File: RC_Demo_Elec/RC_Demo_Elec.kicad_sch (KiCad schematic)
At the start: 4 parts, among them M1 Motor_DC_LEFT, M2 Motor_DC_RIGHT, U1 Nucleo-L152RE

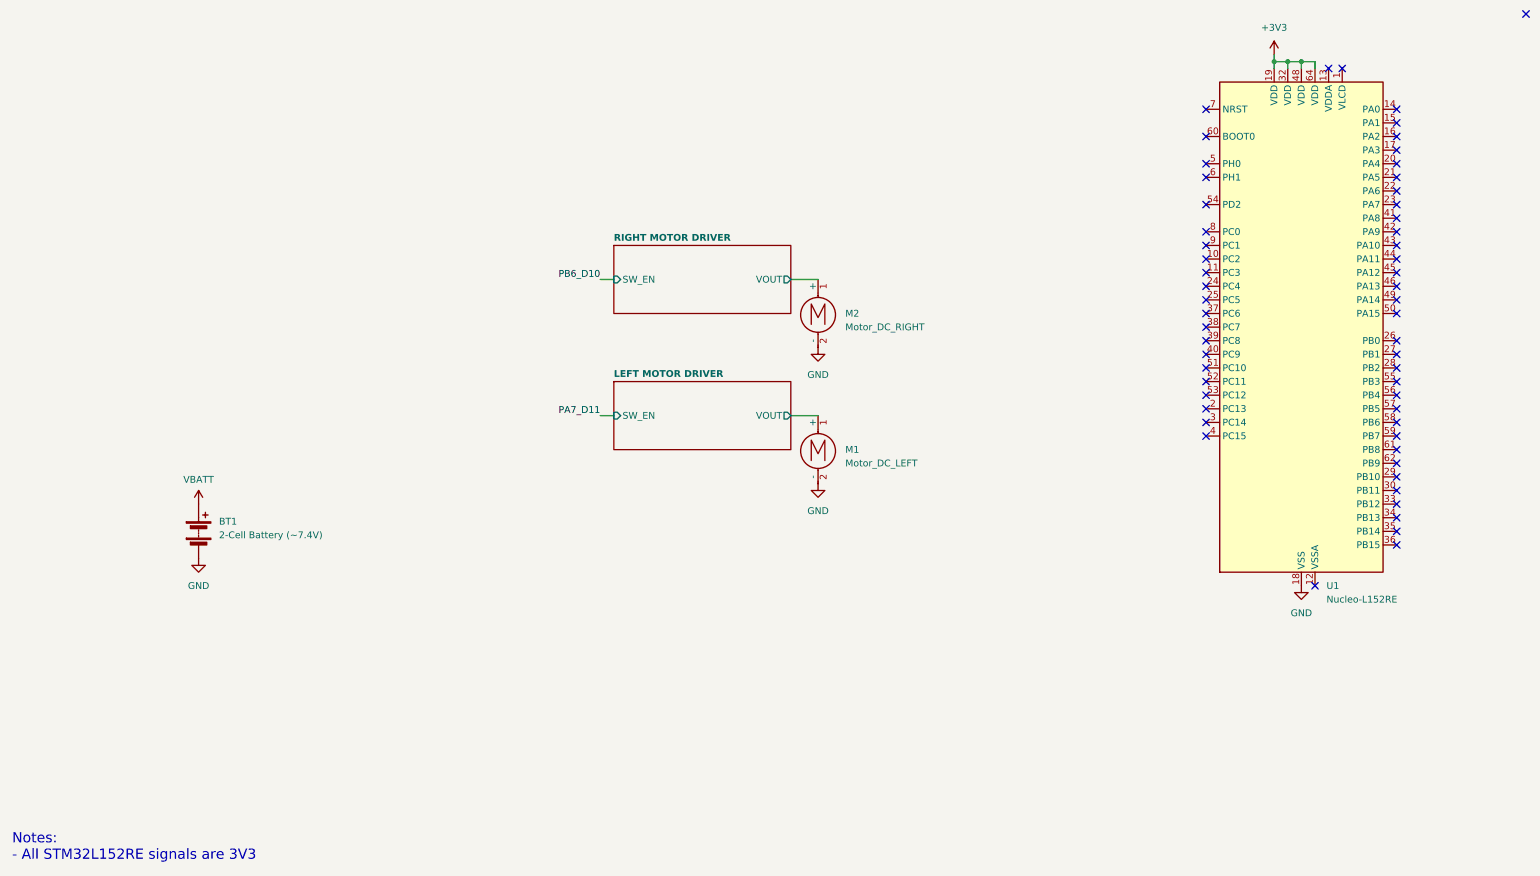
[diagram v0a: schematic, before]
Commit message: [chore] - pin ThetOS to v1.1.0 + commit Cargo.lock + schematic added note
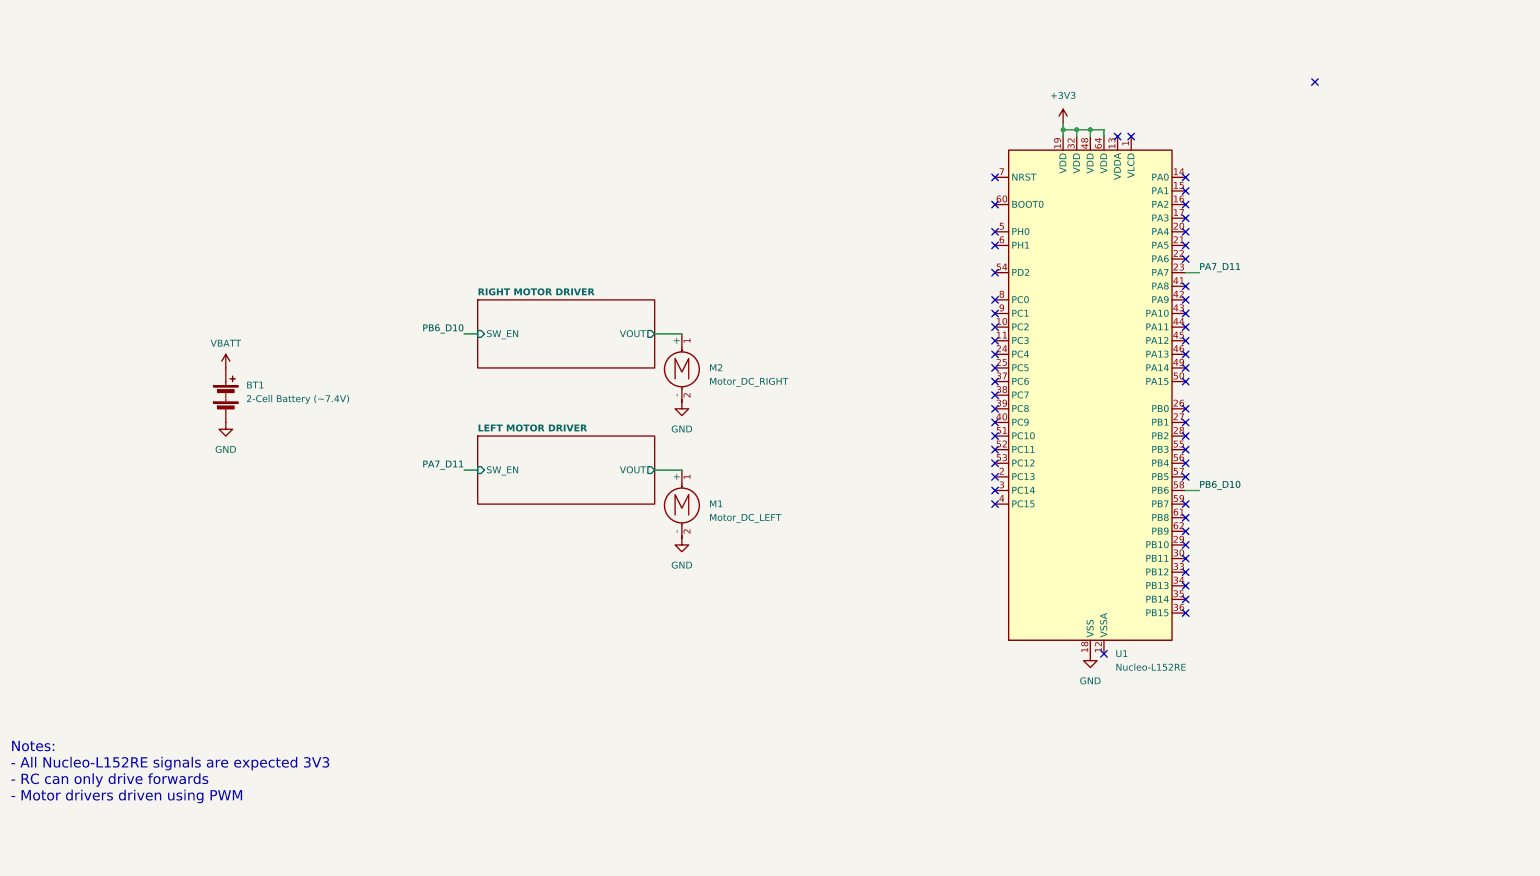
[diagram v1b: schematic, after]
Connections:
- net PA7_D11: now also U1.23 (PA7)
- net PB6_D10: now also U1.58 (PB6)
- no-connect marks 57 -> 55
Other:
- note added: "Notes: - All Nucleo-L152RE signals are expected 3V3 - RC can only drive forwards - Motor drivers driven using PWM"
- note removed: "Notes: - All STM32L152RE signals are 3V3"
- moved on the sheet: BT1, M1, M2, U1
